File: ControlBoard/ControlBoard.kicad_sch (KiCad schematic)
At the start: 11 parts

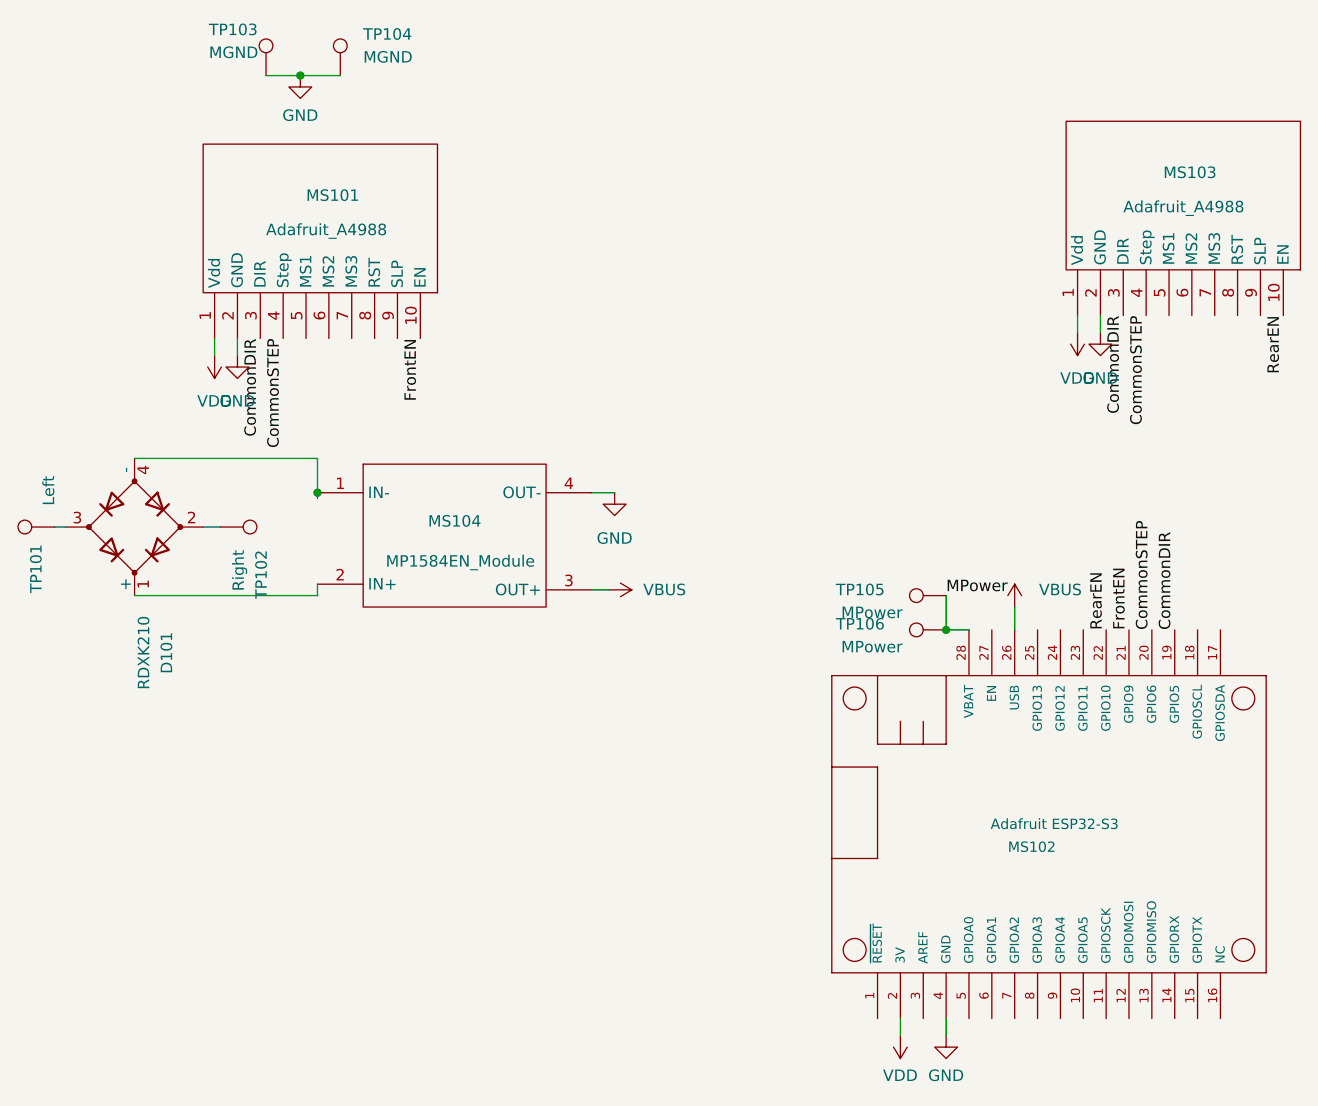
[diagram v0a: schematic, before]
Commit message: Add Sleep. Start on the firmware.
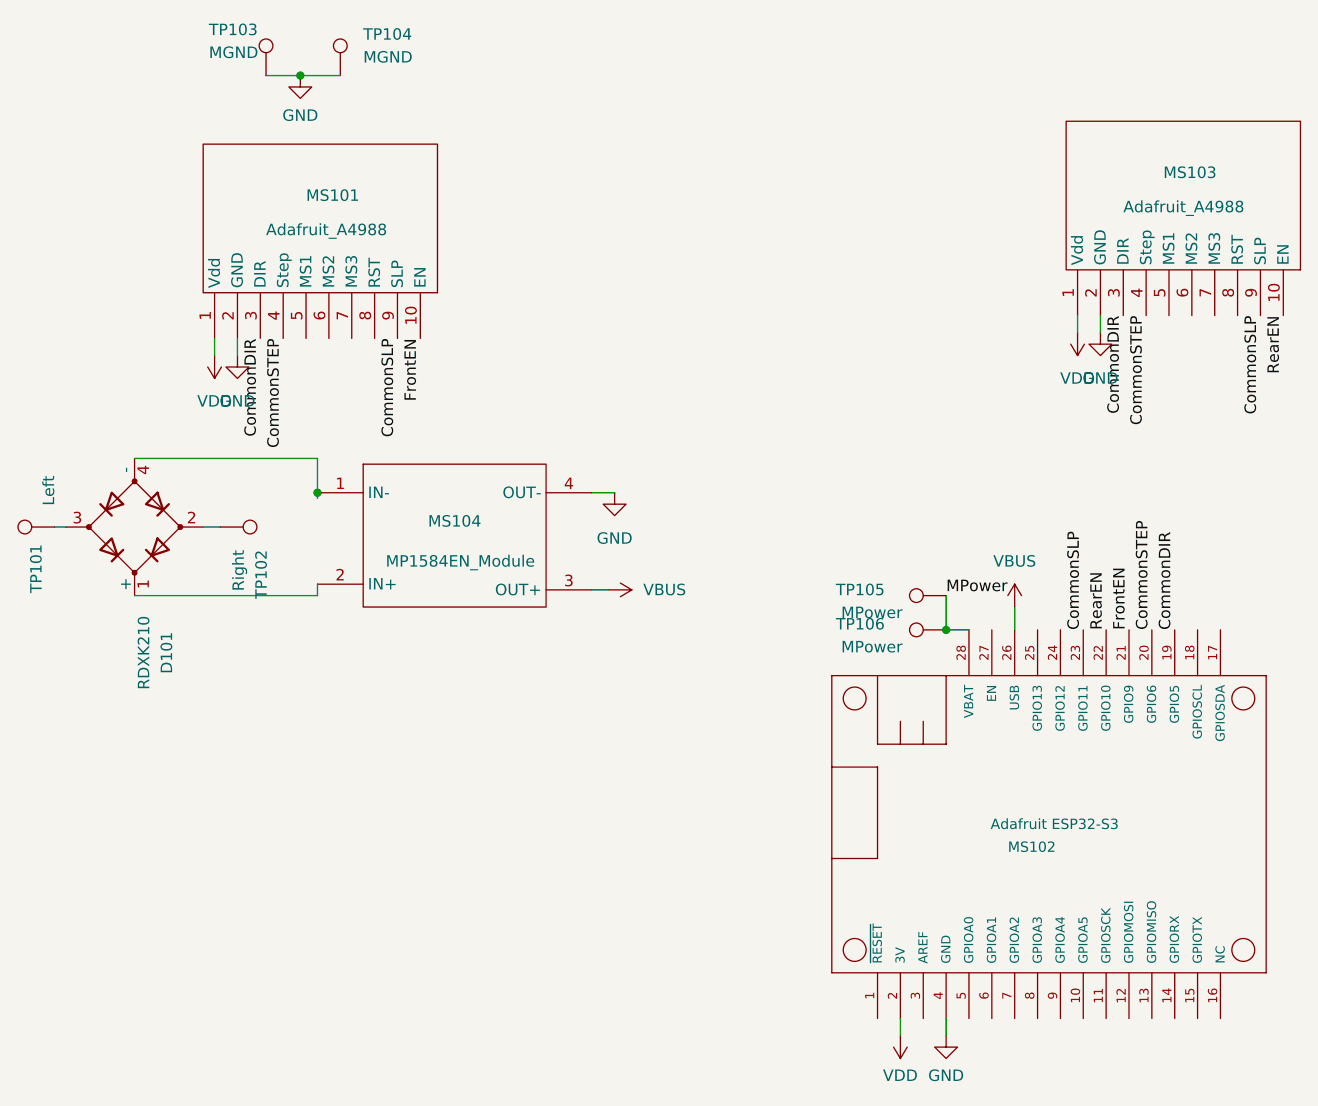
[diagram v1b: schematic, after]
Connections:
- net CommonSLP: now reaches MS102.23 (GPIO11)
- net CommonSLP: now also MS101.9 (SLP), MS103.9 (SLP)
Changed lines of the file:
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@@
+    (effects (font (size 1.27 1.27)) (justify right bottom))
+  )
+  (label "CommonSLP" (at 55.245 59.055 270)
     (effects (font (size 1.27 1.27)) (justify right bottom))
   )
@@
   (label "CommonDIR" (at 141.605 91.44 90)
     (effects (font (size 1.27 1.27)) (justify left bottom))
+  )
+  (label "CommonSLP" (at 151.13 56.515 270)
+    (effects (font (size 1.27 1.27)) (justify right bottom))
   )
   (label "FrontEN" (at 57.785 59.055 270)
@@
   (label "CommonSTEP" (at 42.545 59.055 270)
     (effects (font (size 1.27 1.27)) (justify right bottom))
+  )
+  (label "CommonSLP" (at 131.445 91.44 90)
+    (effects (font (size 1.27 1.27)) (justify left bottom))
   )
   (label "FrontEN" (at 136.525 91.44 90)
@@
       (effects (font (size 1.27 1.27)) hide)
     )
-    (property "Value" "VBUS" (id 1) (at 128.905 86.995 0))
+    (property "Value" "VBUS" (id 1) (at 123.825 83.82 0))
     (property "Footprint" "" (id 2) (at 123.825 88.9 0)
       (effects (font (size 1.27 1.27)) hide)

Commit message: Add Schematic PDF and 3D views of PCB.
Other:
- company: (none) -> Deepwoods Software
- title: (none) -> Boxcar WiFi Coupler Control
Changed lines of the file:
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@@
 (kicad_sch (version 20211123) (generator eeschema)
-  (paper "A4")
+  (paper "USLetter")
+  (title_block
+    (title "Boxcar WiFi Coupler Control")
+    (date "2025-10-31")
+    (rev "A")
+    (company "Deepwoods Software")
+  )
   (junction (at 44.45 29.845) (diameter 0) (color 0 0 0 0)
   )
